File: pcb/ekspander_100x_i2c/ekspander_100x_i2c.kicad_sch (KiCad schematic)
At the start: 13 parts, among them J1 DG127A-5.08-06P-14-00AH, J2 DG127A-5.08-06P-14-00AH, J3 DG127A-5.08-06P-14-00AH, J4 DG127A-5.08-06P-14-00AH, U1 MCP23017_SP, U10 ITS716G, U11 LTV-847, U12 ITS716G, U9 LTV-847

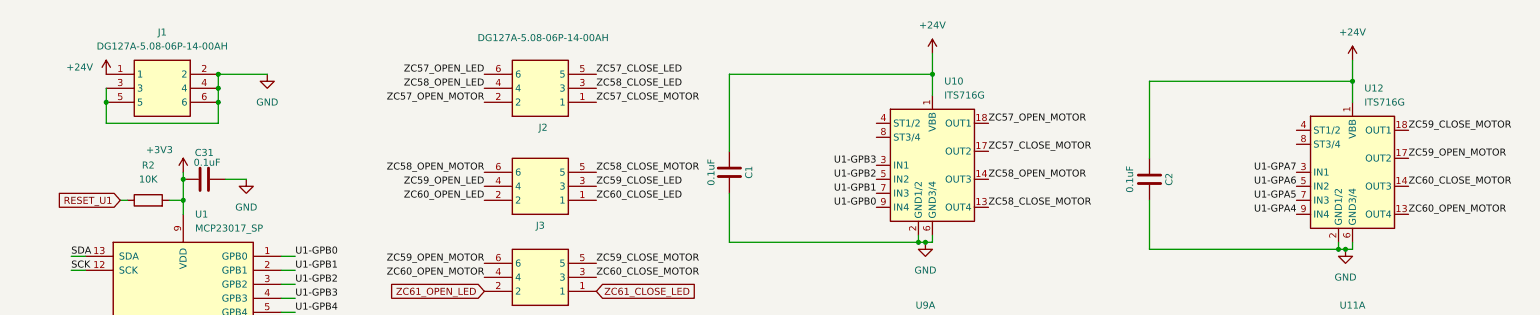
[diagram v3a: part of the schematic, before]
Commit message: Ekspander 100x - PCB layout V2
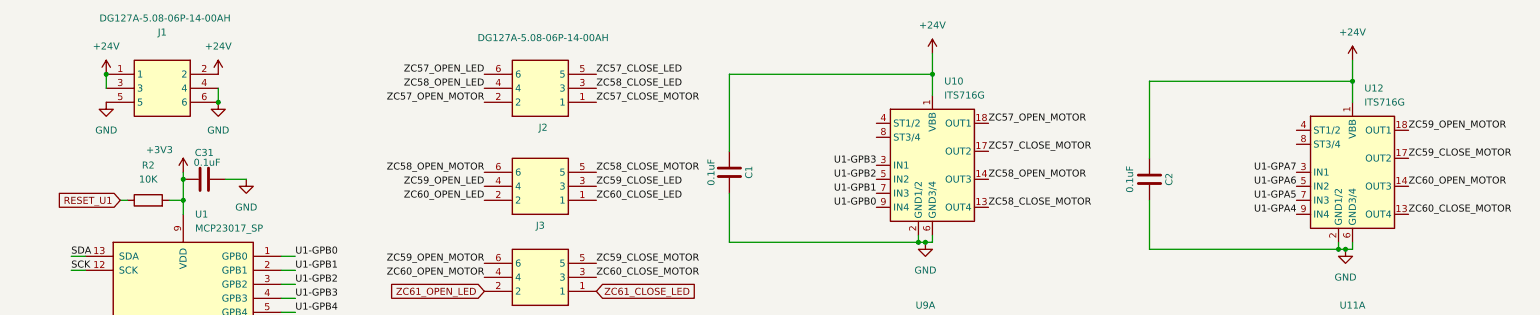
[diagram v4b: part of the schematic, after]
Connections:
- net +24V: now also J1.2, J1.3
- net GND: no longer J1.2, J1.3
- net ZC59_CLOSE_MOTOR: now also U12.17 (OUT2); no longer U12.18 (OUT1)
- net ZC59_OPEN_MOTOR: now also U12.18 (OUT1); no longer U12.17 (OUT2)
- net ZC60_CLOSE_MOTOR: now also U12.13 (OUT4); no longer U12.14 (OUT3)
- net ZC60_OPEN_MOTOR: now also U12.14 (OUT3); no longer U12.13 (OUT4)

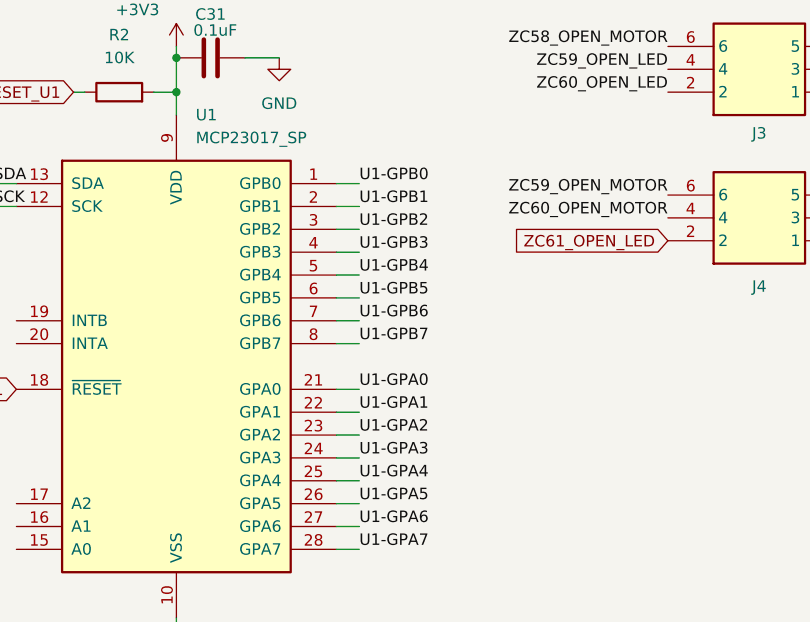
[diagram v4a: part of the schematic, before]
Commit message: Ekspander 100x - rerouting
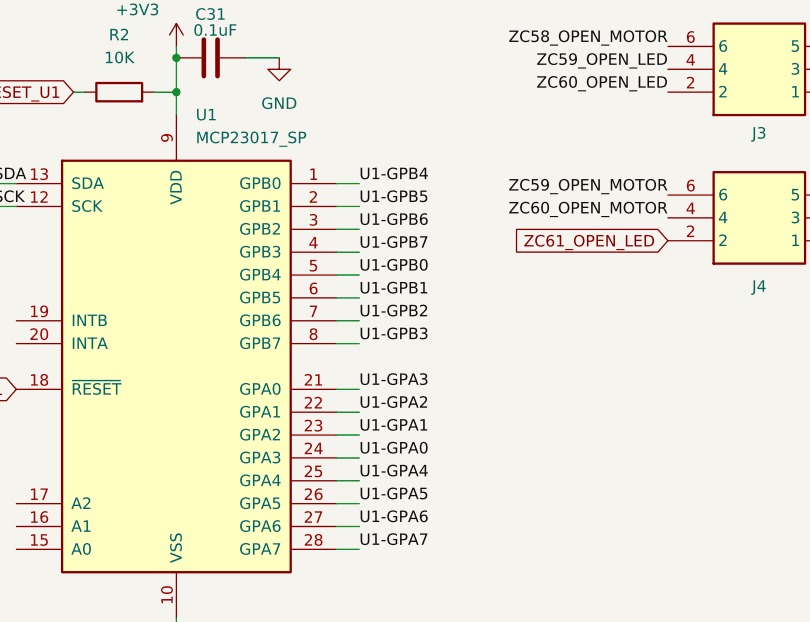
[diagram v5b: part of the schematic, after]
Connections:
- net U1-GPA0: now also U1.24 (GPA3); no longer U1.21 (GPA0)
- net U1-GPA1: now also U1.23 (GPA2); no longer U1.22 (GPA1)
- net U1-GPA2: now also U1.22 (GPA1); no longer U1.23 (GPA2)
- net U1-GPA3: now also U1.21 (GPA0); no longer U1.24 (GPA3)
- net U1-GPB0: now also U1.5 (GPB4); no longer U1.1 (GPB0)
- net U1-GPB1: now also U1.6 (GPB5); no longer U1.2 (GPB1)
- net U1-GPB2: now also U1.7 (GPB6); no longer U1.3 (GPB2)
- net U1-GPB3: now also U1.8 (GPB7); no longer U1.4 (GPB3)
- net U1-GPB4: now also U1.1 (GPB0); no longer U1.5 (GPB4)
- net U1-GPB5: now also U1.2 (GPB1); no longer U1.6 (GPB5)
- net U1-GPB6: now also U1.3 (GPB2); no longer U1.7 (GPB6)
- net U1-GPB7: now also U1.4 (GPB3); no longer U1.8 (GPB7)
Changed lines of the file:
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@@
-		)
-	)
-	(label "U1-GPB5"
-		(at 57.15 69.85 0)
-		(effects
-			(font
-				(size 1.27 1.27)
-			)
-			(justify left bottom)
-		)
-		(property "Netclass" "GPIO"
-			(at 67.056 69.85 0)
-			(effects
-				(font
-					(size 1.27 1.27)
-					(italic yes)
-				)
-				(justify left)
-			)
 		)
 	)
@@
 		)
 	)
-	(label "U1-GPB1"
-		(at 57.15 59.69 0)
-		(effects
-			(font
-				(size 1.27 1.27)
-			)
-			(justify left bottom)
-		)
-		(property "Netclass" "GPIO"
-			(at 67.056 59.69 0)
-			(effects
-				(font
-					(size 1.27 1.27)
-					(italic yes)
-				)
-				(justify left)
-			)
-		)
-	)
 	(label "U1-GPB7"
 		(at 186.69 118.11 0)
@@
 		)
 	)
+	(label "U1-GPB0"
+		(at 57.15 67.31 0)
+		(effects
+			(font
+				(size 1.27 1.27)
+			)
+			(justify left bottom)
+		)
+		(property "Netclass" "GPIO"
+			(at 67.056 67.31 0)
+			(effects
+				(font
+					(size 1.27 1.27)
+					(italic yes)
+				)
+				(justify left)
+			)
+		)
+	)
 	(label "ZC57_OPEN_LED"
 		(at 160.02 118.11 180)
@@
 		)
 	)
-	(label "U1-GPB0"
-		(at 57.15 57.15 0)
-		(effects
-			(font
-				(size 1.27 1.27)
-			)
-			(justify left bottom)
-		)
-		(property "Netclass" "GPIO"
-			(at 67.056 57.15 0)
-			(effects
-				(font
-					(size 1.27 1.27)
-					(italic yes)
-				)
-				(justify left)
-			)
-		)
-	)
 	(label "U1-GPA6"
 		(at 238.76 44.45 180)
@@
 		)
 	)
+	(label "U1-GPB4"
+		(at 57.15 57.15 0)
+		(effects
+			(font
+				(size 1.27 1.27)
+			)
+			(justify left bottom)
+		)
+		(property "Netclass" "GPIO"
+			(at 67.31 57.15 0)
+			(effects
+				(font
+					(size 1.27 1.27)
+					(italic yes)
+				)
+				(justify left)
+			)
+		)
+	)
 	(label "ZC59_OPEN_LED"
 		(at 237.49 118.11 180)
@@
 		)
 	)
-	(label "U1-GPB2"
-		(at 57.15 62.23 0)
-		(effects
-			(font
-				(size 1.27 1.27)
-			)
-			(justify left bottom)
-		)
-		(property "Netclass" "GPIO"
-			(at 67.056 62.23 0)
-			(effects
-				(font
-					(size 1.27 1.27)
-					(italic yes)
-				)
-				(justify left)
-			)
-		)
-	)
 	(label "ZC57_CLOSE_MOTOR"
 		(at 111.76 29.21 0)
@@
 	)
 	(label "U1-GPA0"
-		(at 57.15 80.01 0)
-		(effects
-			(font
-				(size 1.27 1.27)
-			)
-			(justify left bottom)
-		)
-		(property "Netclass" "GPIO"
-			(at 67.31 80.01 0)
+		(at 57.15 87.63 0)
+		(effects
+			(font
+				(size 1.27 1.27)
+			)
+			(justify left bottom)
+		)
+		(property "Netclass" "GPIO"
+			(at 67.31 87.63 0)
 			(effects
 				(font
@@
 	)
 	(label "U1-GPA2"
-		(at 57.15 85.09 0)
-		(effects
-			(font
-				(size 1.27 1.27)
-			)
-			(justify left bottom)
-		)
-		(property "Netclass" "GPIO"
-			(at 67.056 85.09 0)
+		(at 57.15 82.55 0)
+		(effects
+			(font
+				(size 1.27 1.27)
+			)
+			(justify left bottom)
+		)
+		(property "Netclass" "GPIO"
+			(at 67.056 82.55 0)
+			(effects
+				(font
+					(size 1.27 1.27)
+					(italic yes)
+				)
+				(justify left)
+			)
+		)
+	)
+	(label "U1-GPB7"
+		(at 57.15 64.77 0)
+		(effects
+			(font
+				(size 1.27 1.27)
+			)
+			(justify left bottom)
+		)
+		(property "Netclass" "GPIO"
+			(at 67.056 64.77 0)
+			(effects
+				(font
+					(size 1.27 1.27)
+					(italic yes)
+				)
+				(justify left)
+			)
+		)
+	)
+	(label "U1-GPB1"
+		(at 57.15 69.85 0)
+		(effects
+			(font
+				(size 1.27 1.27)
+			)
+			(justify left bottom)
+		)
+		(property "Netclass" "GPIO"
+			(at 67.056 69.85 0)
 			(effects
 				(font
@@
 		)
 	)
-	(label "U1-GPB7"
-		(at 57.15 74.93 0)
-		(effects
-			(font
-				(size 1.27 1.27)
-			)
-			(justify left bottom)
-		)
-		(property "Netclass" "GPIO"
-			(at 67.056 74.93 0)
+	(label "U1-GPB6"
+		(at 57.15 62.23 0)
+		(effects
+			(font
+				(size 1.27 1.27)
+			)
+			(justify left bottom)
+		)
+		(property "Netclass" "GPIO"
+			(at 67.056 62.23 0)
+			(effects
+				(font
+					(size 1.27 1.27)
+					(italic yes)
+				)
+				(justify left)
+			)
+		)
+	)
+	(label "U1-GPB2"
+		(at 57.15 72.39 0)
+		(effects
+			(font
+				(size 1.27 1.27)
+			)
+			(justify left bottom)
+		)
+		(property "Netclass" "GPIO"
+			(at 67.056 72.39 0)
 			(effects
 				(font
@@
 		)
 	)
-	(label "U1-GPB4"
-		(at 57.15 67.31 0)
-		(effects
-			(font
-				(size 1.27 1.27)
-			)
-			(justify left bottom)
-		)
-		(property "Netclass" "GPIO"
-			(at 67.31 67.31 0)
-			(effects
-				(font
-					(size 1.27 1.27)
-					(italic yes)
-				)
-				(justify left)
-			)
-		)
-	)
 	(label "U1-GPA4"
 		(at 238.76 49.53 180)
@@
 		)
 	)
-	(label "U1-GPB6"
-		(at 57.15 72.39 0)
-		(effects
-			(font
-				(size 1.27 1.27)
-			)
-			(justify left bottom)
-		)
-		(property "Netclass" "GPIO"
-			(at 67.056 72.39 0)
-			(effects
-				(font
-					(size 1.27 1.27)
-					(italic yes)
-				)
-				(justify left)
-			)
-		)
-	)
 	(label "ZC57_OPEN_MOTOR"
 		(at 91.44 29.21 180)
@@
 				)
 				(justify right)
-			)
-		)
-	)
-	(label "U1-GPB3"
-		(at 57.15 64.77 0)
-		(effects
-			(font
-				(size 1.27 1.27)
-			)
-			(justify left bottom)
-		)
-		(property "Netclass" "GPIO"
-			(at 67.056 64.77 0)
-			(effects
-				(font
-					(size 1.27 1.27)
-					(italic yes)
-				)
-				(justify left)
 			)
 		)
@@
 	)
 	(label "U1-GPA3"
-		(at 57.15 87.63 0)
-		(effects
-			(font
-				(size 1.27 1.27)
-			)
-			(justify left bottom)
-		)
-		(property "Netclass" "GPIO"
-			(at 67.056 87.63 0)
+		(at 57.15 80.01 0)
+		(effects
+			(font
+				(size 1.27 1.27)
+			)
+			(justify left bottom)
+		)
+		(property "Netclass" "GPIO"
+			(at 67.056 80.01 0)
 			(effects
 				(font
@@
 		)
 	)
+	(label "U1-GPB3"
+		(at 57.15 74.93 0)
+		(effects
+			(font
+				(size 1.27 1.27)
+			)
+			(justify left bottom)
+		)
+		(property "Netclass" "GPIO"
+			(at 67.056 74.93 0)
+			(effects
+				(font
+					(size 1.27 1.27)
+					(italic yes)
+				)
+				(justify left)
+			)
+		)
+	)
+	(label "U1-GPB5"
+		(at 57.15 59.69 0)
+		(effects
+			(font
+				(size 1.27 1.27)
+			)
+			(justify left bottom)
+		)
+		(property "Netclass" "GPIO"
+			(at 67.056 59.69 0)
+			(effects
+				(font
+					(size 1.27 1.27)
+					(italic yes)
+				)
+				(justify left)
+			)
+		)
+	)
 	(label "U1-GPA5"
 		(at 238.76 46.99 180)
@@
 	)
 	(label "U1-GPA1"
-		(at 57.15 82.55 0)
-		(effects
-			(font
-				(size 1.27 1.27)
-			)
-			(justify left bottom)
-		)
-		(property "Netclass" "GPIO"
-			(at 67.31 82.55 0)
-			(effects
-				(font
+		(at 57.15 85.09 0)
+		(effects
+			(font
+				(size 1.27 1.27)
+			)
+			(justify left bottom)
+		)
+		(property "Netclass" "GPIO"
+			(at 67.31 85.09 0)
+			(effects
+				(font

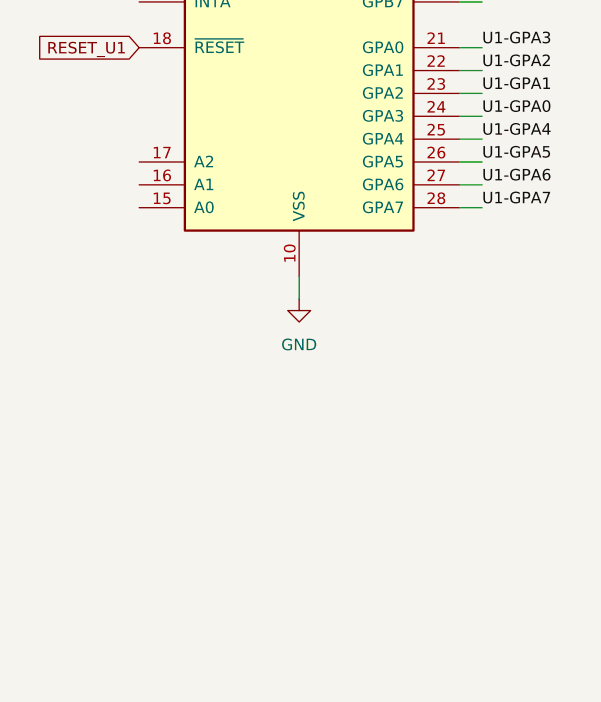
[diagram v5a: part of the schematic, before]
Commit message: Ekspander 100x - adresacja I2C - MCP23017
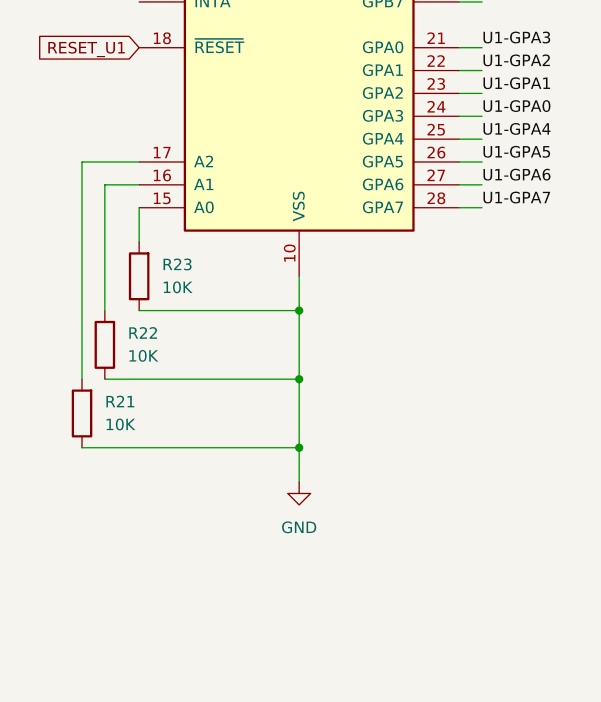
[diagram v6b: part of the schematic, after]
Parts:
- added R21, R22, R23: 10K, PCM_Resistor_SMD_AKL:R_0805_2012Metric_Pad1.20x1.40mm_HandSolder, symbol Device:R
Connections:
- net GND: now also R21.1, R22.1, R23.1
- net at U1.15 (A0): now also R23.2
- net at U1.16 (A1): now also R22.2
- net at U1.17 (A2): now also R21.2

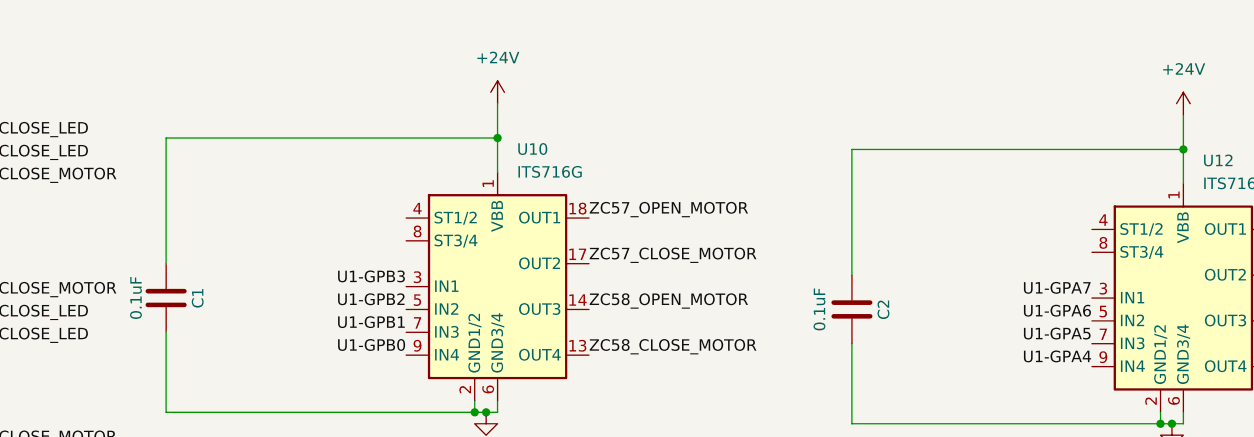
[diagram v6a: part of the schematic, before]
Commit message: Ekspander 100x - diagnostic LEDs
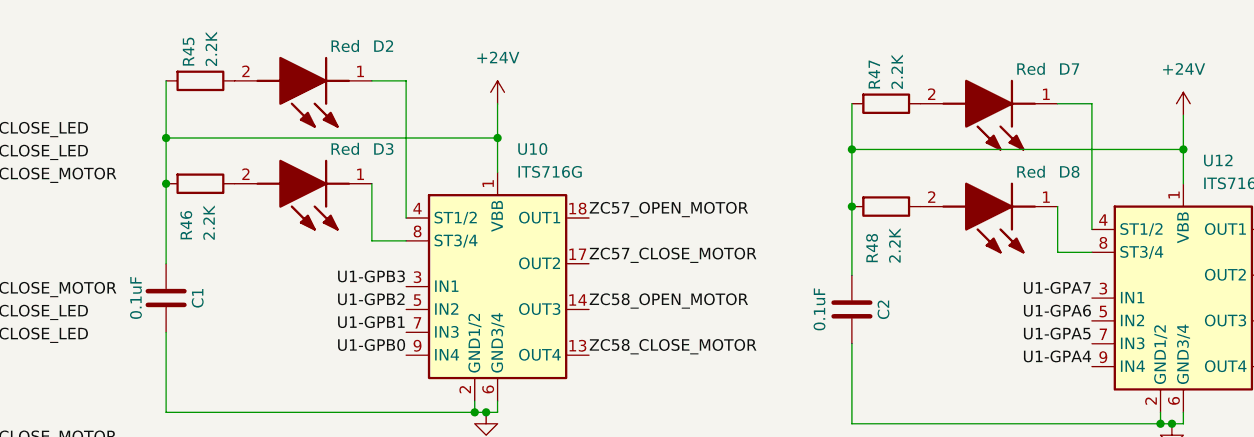
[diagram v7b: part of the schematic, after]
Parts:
- added D2, D3, D7, D8: Red, 1_tme:LEDC2012X120N, symbol LTST-C170KRKT:LTST-C170KRKT
- added R45, R46, R47, R48: 2.2K, PCM_Resistor_SMD_AKL:R_0805_2012Metric_Pad1.20x1.40mm_HandSolder, symbol Device:R
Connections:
- net +24V: now also R45.2, R46.2, R47.2, R48.2
- net at U12.4 (ST1/2): now also D7.1 (K)
- net at U12.8 (ST3/4): now also D8.1 (K)
- net at U10.4 (ST1/2): now also D2.1 (K)
- net at U10.8 (ST3/4): now also D3.1 (K)
- new net: D3.2 (A), R46.1
- new net: D2.2 (A), R45.1
- new net: D8.2 (A), R48.1
- new net: D7.2 (A), R47.1
